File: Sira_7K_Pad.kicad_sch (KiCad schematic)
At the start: 21 parts, among them J1 AVR-ISP-6, SW1 SW_Push, U1 ATmega32U4-A, U2 PRTR5V0U2X, Y1 Crystal_GND24_Small

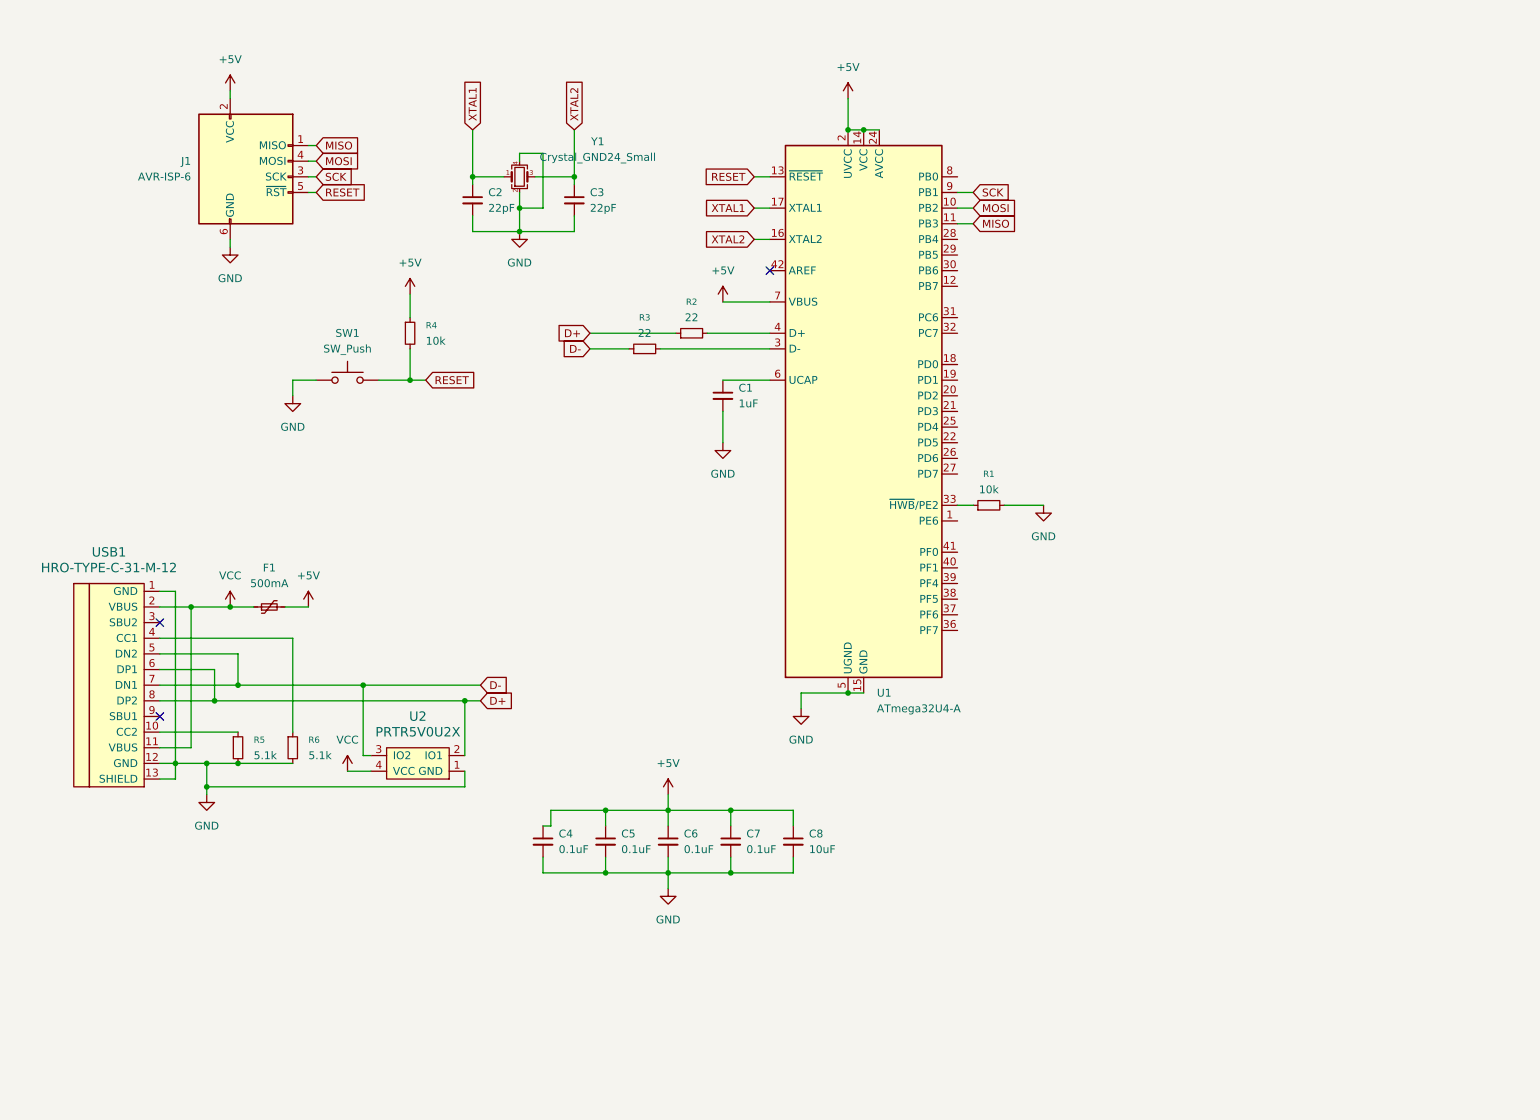
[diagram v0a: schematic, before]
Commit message: started pcb layout
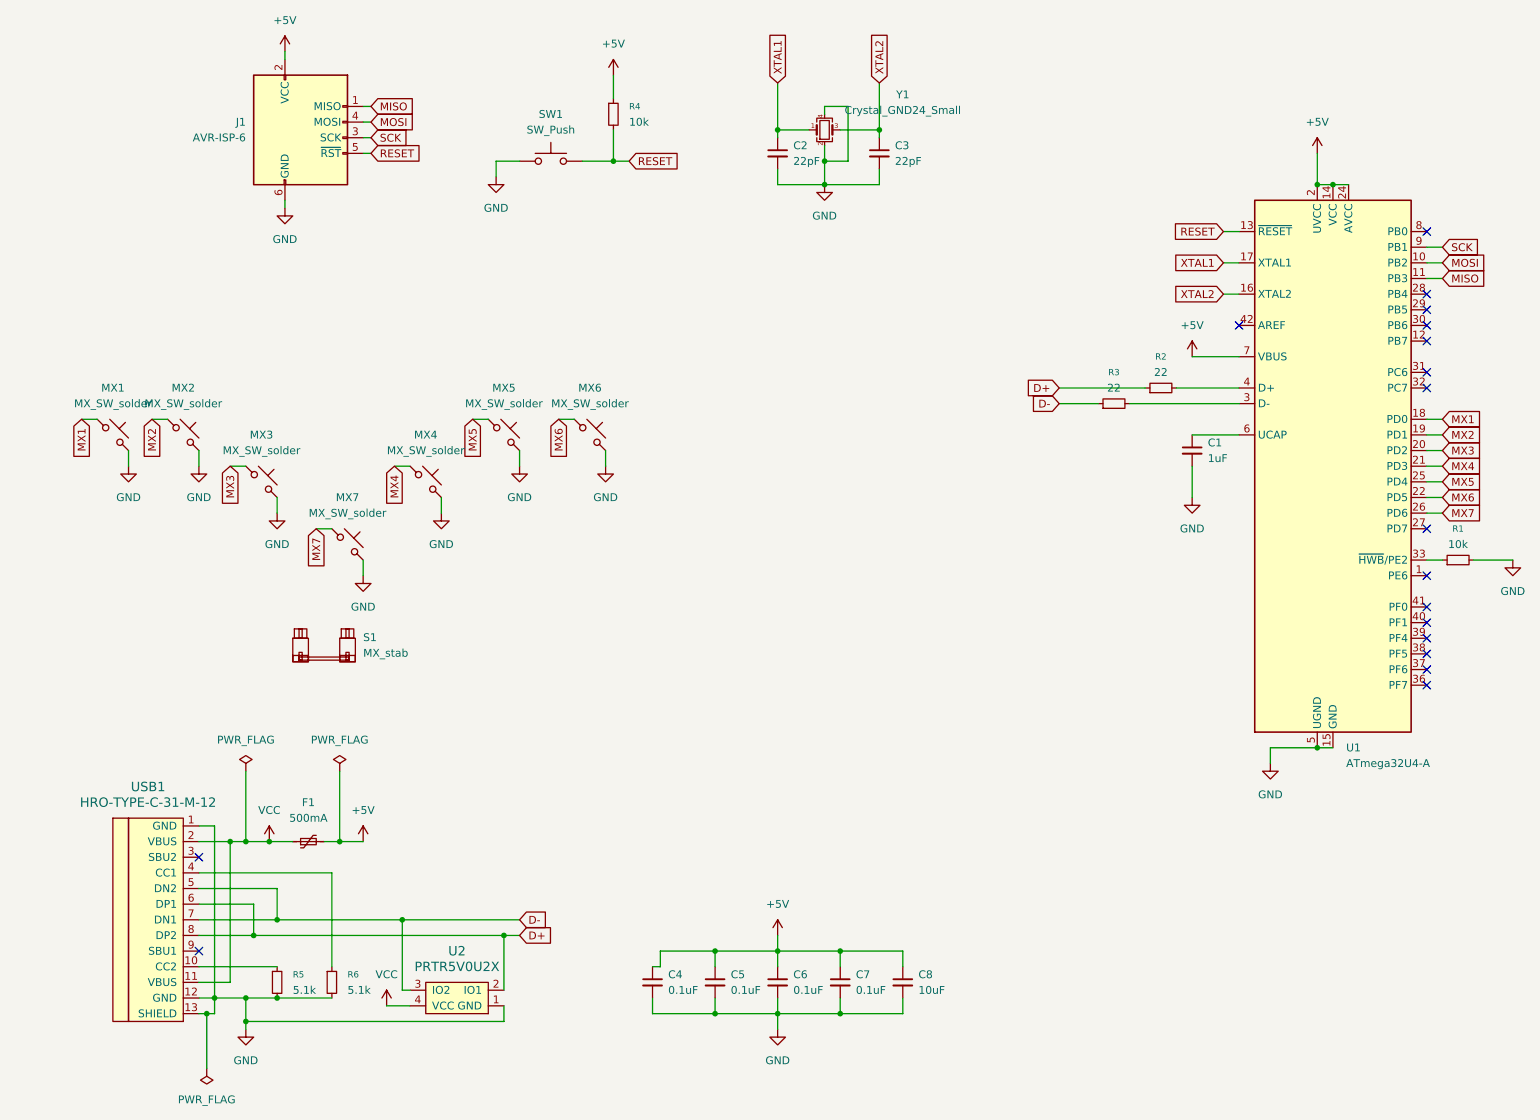
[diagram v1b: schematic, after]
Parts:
- added MX1, MX2, MX3, MX4, MX5, MX6, MX7: MX_SW_solder, marbastlib-mx:SW_MX_1u, symbol marbastlib-mx:MX_SW_solder
- added S1: MX_stab, marbastlib-mx:STAB_MX_P_6.25u, symbol marbastlib-mx:MX_stab
- C1, C2, C3, C4, C5, C6, C7, C8: footprint (none) -> Capacitor_SMD:C_0805_2012Metric
- F1: footprint (none) -> Fuse:Fuse_1206_3216Metric
- J1: footprint (none) -> random-keyboard-parts:Reset_Pretty-Mask
- R1, R2, R3, R4, R5, R6: footprint (none) -> Resistor_SMD:R_0805_2012Metric
- SW1: footprint (none) -> Button_Switch_SMD:SW_SPST_SKQG_WithStem
- U2: footprint (none) -> random-keyboard-parts:SOT143B
- USB1: footprint (none) -> Type-C:HRO-TYPE-C-31-M-12-Assembly
- Y1: footprint (none) -> Crystal:Crystal_SMD_3225-4Pin_3.2x2.5mm
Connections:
- net GND: now also MX1.2, MX2.2, MX3.2, MX4.2, MX5.2, MX6.2, MX7.2
- net MX1: now reaches U1.18 (PD0)
- net MX1: now also MX1.1
- net MX2: now reaches U1.19 (PD1)
- net MX2: now also MX2.1
- net MX3: now reaches U1.20 (PD2)
- net MX3: now also MX3.1
- net MX4: now reaches U1.21 (PD3)
- net MX4: now also MX4.1
- net MX6: now reaches U1.22 (PD5)
- net MX6: now also MX6.1
- net MX5: now reaches U1.25 (PD4)
- net MX5: now also MX5.1
- net MX7: now reaches U1.26 (PD6)
- net MX7: now also MX7.1
- no-connect marks 3 -> 18
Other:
- moved on the sheet: C1, C2, C3, C4, C5, C6, C7, C8, F1, J1, R1, R2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

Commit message: almost finished routing and cleaning up the pcb
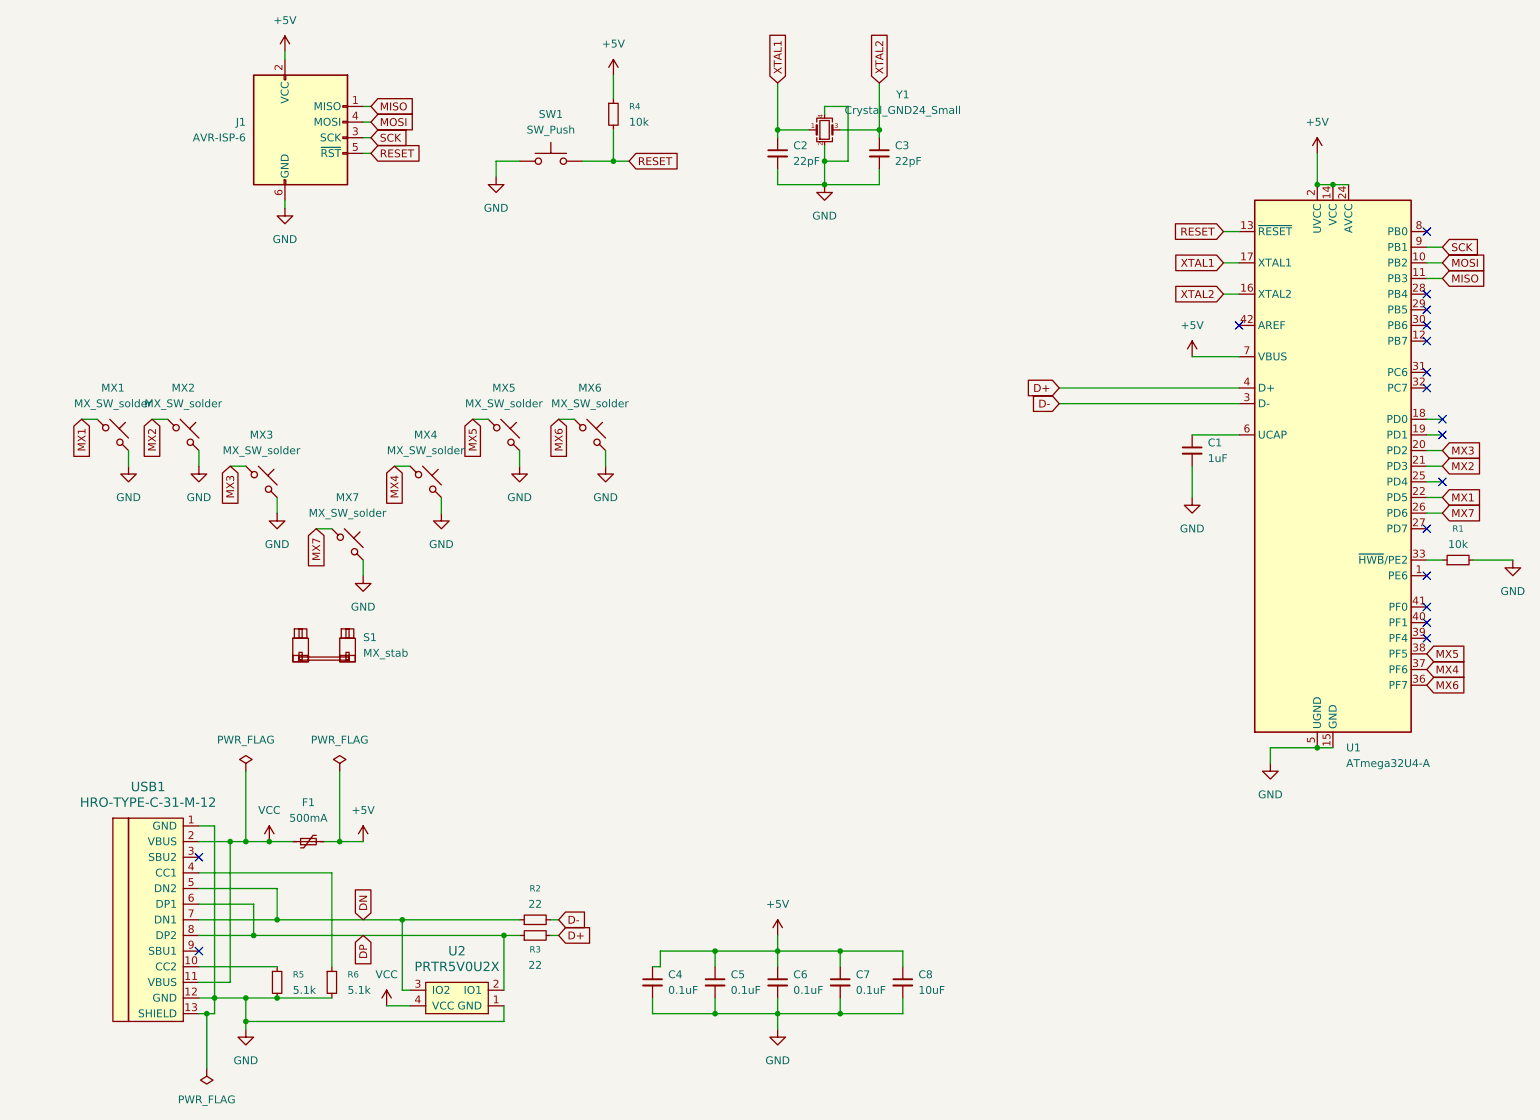
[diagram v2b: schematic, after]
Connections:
- net D+: now also R3.2, U1.4 (D+); no longer R2.1, U2.2 (IO1), USB1.6 (DP1), USB1.8 (DP2)
- net D-: now also R2.2, U1.3 (D-); no longer R3.1, U2.3 (IO2), USB1.5 (DN2), USB1.7 (DN1)
- net MX1: now also U1.22 (PD5); no longer U1.18 (PD0)
- net MX2: now also U1.21 (PD3); no longer U1.19 (PD1)
- net MX4: now also U1.37 (PF6); no longer U1.21 (PD3)
- net MX5: now also U1.38 (PF5); no longer U1.25 (PD4)
- net MX6: now also U1.36 (PF7); no longer U1.22 (PD5)
- new net DN: R2.1, U2.3 (IO2), USB1.5 (DN2), USB1.7 (DN1)
- new net DP: R3.1, U2.2 (IO1), USB1.6 (DP1), USB1.8 (DP2)
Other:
- moved on the sheet: R2, R3
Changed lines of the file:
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@@
 	)
 	(no_connect
-		(at 243.84 123.19)
+		(at 246.38 92.71)
 	)
 	(no_connect
-		(at 243.84 125.73)
+		(at 246.38 85.09)
 	)
 	(no_connect
@@
 	)
 	(no_connect
-		(at 243.84 120.65)
+		(at 246.38 82.55)
 	)
 	(wire
@@
 	(wire
 		(pts
-			(xy 203.2 77.47) (xy 213.36 77.47)
-		)
-		(stroke
-			(width 0)
-			(type default)
-		)
-	)
-	(wire
-		(pts
 			(xy 251.46 105.41) (xy 257.81 105.41)
 		)
@@
 	(wire
 		(pts
+			(xy 101.6 163.83) (xy 102.87 163.83)
+		)
+		(stroke
+			(width 0)
+			(type default)
+		)
+	)
+	(wire
+		(pts
 			(xy 45.72 179.07) (xy 44.45 179.07)
 		)
@@
 	(wire
 		(pts
-			(xy 195.58 80.01) (xy 213.36 80.01)
-		)
-		(stroke
-			(width 0)
-			(type default)
-		)
-	)
-	(wire
-		(pts
 			(xy 93.98 166.37) (xy 96.52 166.37)
 		)
@@
 	(wire
 		(pts
-			(xy 184.15 77.47) (xy 198.12 77.47)
+			(xy 184.15 77.47) (xy 213.36 77.47)
 		)
 		(stroke
@@
 	(wire
 		(pts
-			(xy 184.15 80.01) (xy 190.5 80.01)
+			(xy 184.15 80.01) (xy 213.36 80.01)
 		)
 		(stroke
@@
 	(wire
 		(pts
+			(xy 101.6 166.37) (xy 102.87 166.37)
+		)
+		(stroke
+			(width 0)
+			(type default)
+		)
+	)
+	(wire
+		(pts
 			(xy 210.82 62.23) (xy 213.36 62.23)
 		)
@@
 	(global_label "MX2"
 		(shape input)
-		(at 246.38 85.09 0)
+		(at 246.38 90.17 0)
 		(fields_autoplaced yes)
 		(effects
@@
 		)
 		(property "Intersheetrefs" "${INTERSHEET_REFS}"
-			(at 253.2356 85.09 0)
+			(at 253.2356 90.17 0)
 			(effects
 				(font
@@
 		)
 	)
+	(global_label "DP"
+		(shape input)
+		(at 71.12 166.37 270)
+		(fields_autoplaced yes)
+		(effects
+			(font
+				(size 1.27 1.27)
+			)
+			(justify right)
+		)
+		(property "Intersheetrefs" "${INTERSHEET_REFS}"
+			(at 71.12 171.8952 90)
+			(effects
+				(font
+					(size 1.27 1.27)
+				)
+				(justify right)
+				(hide yes)
+			)
+		)
+	)
 	(global_label "MX7"
 		(shape input)
@@
 	(global_label "MX5"
 		(shape input)
-		(at 246.38 92.71 0)
+		(at 243.84 120.65 0)
+		(fields_autoplaced yes)
+		(effects
+			(font
+				(size 1.27 1.27)
+			)
+			(justify left)
+		)
+		(property "Intersheetrefs" "${INTERSHEET_REFS}"
+			(at 250.6956 120.65 0)
+			(effects
+				(font
+					(size 1.27 1.27)
+				)
+				(justify left)
+				(hide yes)
+			)
+		)
+	)
+	(global_label "DN"
+		(shape input)
+		(at 71.12 163.83 90)
 		(fields_autoplaced yes)
 		(effects
@@
 		)
 		(property "Intersheetrefs" "${INTERSHEET_REFS}"
-			(at 253.2356 92.71 0)
+			(at 71.12 158.2443 90)
 			(effects
 				(font
@@
 	(global_label "MX4"
 		(shape input)
-		(at 246.38 90.17 0)
+		(at 243.84 123.19 0)
 		(fields_autoplaced yes)
 		(effects
@@
 		)
 		(property "Intersheetrefs" "${INTERSHEET_REFS}"
-			(at 253.2356 90.17 0)
+			(at 250.6956 123.19 0)
 			(effects
 				(font
@@
 	(global_label "MX6"
 		(shape input)
-		(at 246.38 95.25 0)
+		(at 243.84 125.73 0)
 		(fields_autoplaced yes)
 		(effects
@@
 		)
 		(property "Intersheetrefs" "${INTERSHEET_REFS}"
-			(at 253.2356 95.25 0)
+			(at 250.6956 125.73 0)
 			(effects
 				(font
@@
 	(global_label "D+"
 		(shape input)
-		(at 96.52 166.37 0)
+		(at 102.87 166.37 0)
 		(fields_autoplaced yes)
 		(effects
@@
 		)
 		(property "Intersheetrefs" "${INTERSHEET_REFS}"
-			(at 102.3476 166.37 0)
+			(at 108.6976 166.37 0)
 			(effects
 				(font
@@
 	(global_label "MX1"
 		(shape input)
-		(at 246.38 82.55 0)
+		(at 246.38 95.25 0)
 		(fields_autoplaced yes)
 		(effects
@@
 		)
 		(property "Intersheetrefs" "${INTERSHEET_REFS}"
-			(at 253.2356 82.55 0)
+			(at 253.2356 95.25 0)
 			(effects
 				(font
@@
 	(global_label "D-"
 		(shape input)
-		(at 96.52 163.83 0)
+		(at 102.87 163.83 0)
 		(fields_autoplaced yes)
 		(effects
@@
 		)
 		(property "Intersheetrefs" "${INTERSHEET_REFS}"
-			(at 102.3476 163.83 0)
+			(at 108.6976 163.83 0)
 			(effects
 				(font
@@
 	(symbol
 		(lib_id "Device:R_Small")
-		(at 200.66 77.47 90)
+		(at 99.06 163.83 90)
 		(unit 1)
 		(exclude_from_sim no)
@@
 		(fields_autoplaced yes)
 		(property "Reference" "R2"
-			(at 200.66 72.39 90)
+			(at 99.06 158.75 90)
 			(effects
 				(font
@@
 		)
 		(property "Value" "22"
-			(at 200.66 74.93 90)
+			(at 99.06 161.29 90)
 			(effects
 				(font
@@
 		)
 		(property "Footprint" "Resistor_SMD:R_0805_2012Metric"
-			(at 200.66 77.47 0)
+			(at 99.06 163.83 0)
 			(effects
 				(font
@@
 		)
 		(property "Datasheet" "~"
-			(at 200.66 77.47 0)
+			(at 99.06 163.83 0)
 			(effects
 				(font
@@
 		)
 		(property "Description" "Resistor, small symbol"
-			(at 200.66 77.47 0)
+			(at 99.06 163.83 0)
 			(effects
 				(font
@@
 	(symbol
 		(lib_id "Device:R_Small")
-		(at 193.04 80.01 90)
+		(at 99.06 166.37 90)
 		(unit 1)
 		(exclude_from_sim no)
@@
 		(on_board yes)
 		(dnp no)
-		(fields_autoplaced yes)
 		(property "Reference" "R3"
-			(at 193.04 74.93 90)
+			(at 99.06 168.656 90)
 			(effects
 				(font
@@
 		)
 		(property "Value" "22"
-			(at 193.04 77.47 90)
+			(at 99.06 171.196 90)
 			(effects
 				(font
@@
 		)
 		(property "Footprint" "Resistor_SMD:R_0805_2012Metric"
-			(at 193.04 80.01 0)
+			(at 99.06 166.37 0)
 			(effects
 				(font
@@
 		)
 		(property "Datasheet" "~"
-			(at 193.04 80.01 0)
+			(at 99.06 166.37 0)
 			(effects
 				(font
@@
 		)
 		(property "Description" "Resistor, small symbol"
-			(at 193.04 80.01 0)
+			(at 99.06 166.37 0)
 			(effects
 				(font

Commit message: finished (first version) pbc
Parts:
- added FB1: 60@100MHz, Inductor_SMD:L_0805_2012Metric, symbol Device:FerriteBead_Small
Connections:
- net GND: now also FB1.2
- new net Earth: FB1.1

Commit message: idk
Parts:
- C1, C2, C3, C4, C5, C6, C7, C8: footprint Capacitor_SMD:C_0805_2012Metric -> Capacitor_SMD:C_0805_2012Metric_Pad1.18x1.45mm_HandSolder
- F1: footprint Fuse:Fuse_1206_3216Metric -> Fuse:Fuse_1206_3216Metric_Pad1.42x1.75mm_HandSolder
- FB1: footprint Inductor_SMD:L_0805_2012Metric -> Inductor_SMD:L_0805_2012Metric_Pad1.05x1.20mm_HandSolder
- R1, R2, R3, R4, R5, R6: footprint Resistor_SMD:R_0805_2012Metric -> Resistor_SMD:R_0805_2012Metric_Pad1.20x1.40mm_HandSolder
- USB1: footprint Type-C:HRO-TYPE-C-31-M-12-Assembly -> Type-C:HRO-TYPE-C-31-M-12-HandSoldering
- Y1: footprint Crystal:Crystal_SMD_3225-4Pin_3.2x2.5mm -> Crystal:Crystal_SMD_3225-4Pin_3.2x2.5mm_HandSoldering
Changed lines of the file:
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@@
 			)
 		)
-		(property "Footprint" "Resistor_SMD:R_0805_2012Metric"
+		(property "Footprint" "Resistor_SMD:R_0805_2012Metric_Pad1.20x1.40mm_HandSolder"
 			(at 66.04 173.99 0)
 			(effects
@@
 			)
 		)
-		(property "Footprint" "Capacitor_SMD:C_0805_2012Metric"
+		(property "Footprint" "Capacitor_SMD:C_0805_2012Metric_Pad1.18x1.45mm_HandSolder"
 			(at 128.27 173.99 0)
 			(effects
@@
 			)
 		)
-		(property "Footprint" "Capacitor_SMD:C_0805_2012Metric"
+		(property "Footprint" "Capacitor_SMD:C_0805_2012Metric_Pad1.18x1.45mm_HandSolder"
 			(at 154.94 39.37 0)
 			(effects
@@
 			)
 		)
-		(property "Footprint" "Resistor_SMD:R_0805_2012Metric"
+		(property "Footprint" "Resistor_SMD:R_0805_2012Metric_Pad1.20x1.40mm_HandSolder"
 			(at 99.06 163.83 0)
 			(effects
@@
 			)
 		)
-		(property "Footprint" "Resistor_SMD:R_0805_2012Metric"
+		(property "Footprint" "Resistor_SMD:R_0805_2012Metric_Pad1.20x1.40mm_HandSolder"
 			(at 57.15 173.99 0)
 			(effects
@@
 			)
 		)
-		(property "Footprint" "Resistor_SMD:R_0805_2012Metric"
+		(property "Footprint" "Resistor_SMD:R_0805_2012Metric_Pad1.20x1.40mm_HandSolder"
 			(at 99.06 166.37 0)
 			(effects
@@
 			)
 		)
-		(property "Footprint" "Crystal:Crystal_SMD_3225-4Pin_3.2x2.5mm"
+		(property "Footprint" "Crystal:Crystal_SMD_3225-4Pin_3.2x2.5mm_HandSoldering"
 			(at 146.05 35.56 0)
 			(effects
@@
 			)
 		)
-		(property "Footprint" "Capacitor_SMD:C_0805_2012Metric"
+		(property "Footprint" "Capacitor_SMD:C_0805_2012Metric_Pad1.18x1.45mm_HandSolder"
 			(at 118.11 173.99 0)
 			(effects
@@
 			)
 		)
-		(property "Footprint" "Type-C:HRO-TYPE-C-31-M-12-Assembly"
+		(property "Footprint" "Type-C:HRO-TYPE-C-31-M-12-HandSoldering"
 			(at 41.91 162.56 0)
 			(effects
@@
 			)
 		)
-		(property "Footprint" "Capacitor_SMD:C_0805_2012Metric"
+		(property "Footprint" "Capacitor_SMD:C_0805_2012Metric_Pad1.18x1.45mm_HandSolder"
 			(at 148.59 173.99 0)
 			(effects
@@
 			)
 		)
-		(property "Footprint" "Capacitor_SMD:C_0805_2012Metric"
+		(property "Footprint" "Capacitor_SMD:C_0805_2012Metric_Pad1.18x1.45mm_HandSolder"
 			(at 138.43 173.99 0)
 			(effects
@@
 			)
 		)
-		(property "Footprint" "Capacitor_SMD:C_0805_2012Metric"
+		(property "Footprint" "Capacitor_SMD:C_0805_2012Metric_Pad1.18x1.45mm_HandSolder"
 			(at 158.75 173.99 0)
 			(effects
@@
 			)
 		)
-		(property "Footprint" "Fuse:Fuse_1206_3216Metric"
+		(property "Footprint" "Fuse:Fuse_1206_3216Metric_Pad1.42x1.75mm_HandSolder"
 			(at 67.31 149.86 0)
 			(effects
@@
 			)
 		)
-		(property "Footprint" "Inductor_SMD:L_0805_2012Metric"
+		(property "Footprint" "Inductor_SMD:L_0805_2012Metric_Pad1.05x1.20mm_HandSolder"
 			(at 92.71 138.938 90)
 			(effects
@@
 			)
 		)
-		(property "Footprint" "Capacitor_SMD:C_0805_2012Metric"
+		(property "Footprint" "Capacitor_SMD:C_0805_2012Metric_Pad1.18x1.45mm_HandSolder"
 			(at 138.43 39.37 0)
 			(effects
@@
 			)
 		)
-		(property "Footprint" "Resistor_SMD:R_0805_2012Metric"
+		(property "Footprint" "Resistor_SMD:R_0805_2012Metric_Pad1.20x1.40mm_HandSolder"
 			(at 248.92 105.41 0)
 			(effects
@@
 			)
 		)
-		(property "Footprint" "Resistor_SMD:R_0805_2012Metric"
+		(property "Footprint" "Resistor_SMD:R_0805_2012Metric_Pad1.20x1.40mm_HandSolder"
 			(at 111.76 33.02 0)
 			(effects
@@
 			)
 		)
-		(property "Footprint" "Capacitor_SMD:C_0805_2012Metric"
+		(property "Footprint" "Capacitor_SMD:C_0805_2012Metric_Pad1.18x1.45mm_HandSolder"
 			(at 205.74 87.63 0)
 			(effects
